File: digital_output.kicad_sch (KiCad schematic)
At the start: 13 parts, among them J4 Molex MicroFit 2x2, Q13 PMOS, Q9 PMOS

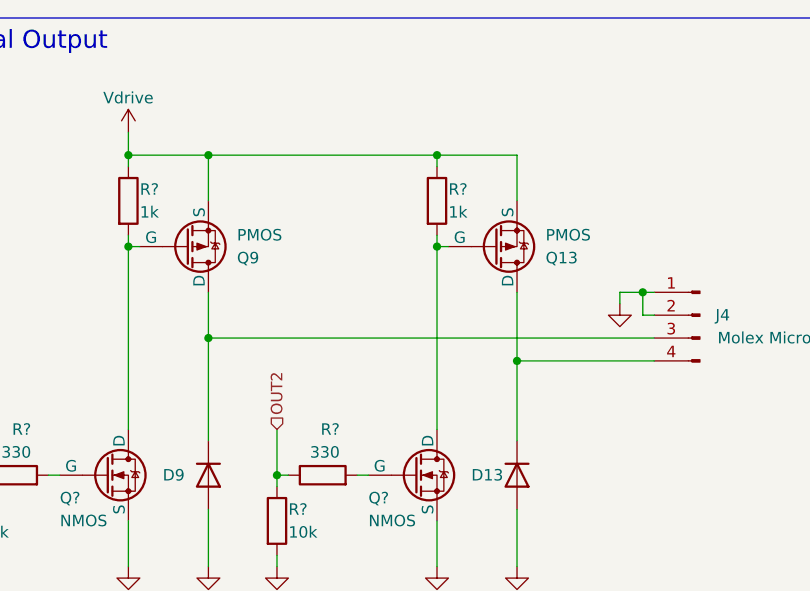
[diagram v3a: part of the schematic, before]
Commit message: updates to the schematics, rough component placement in the PCB layout
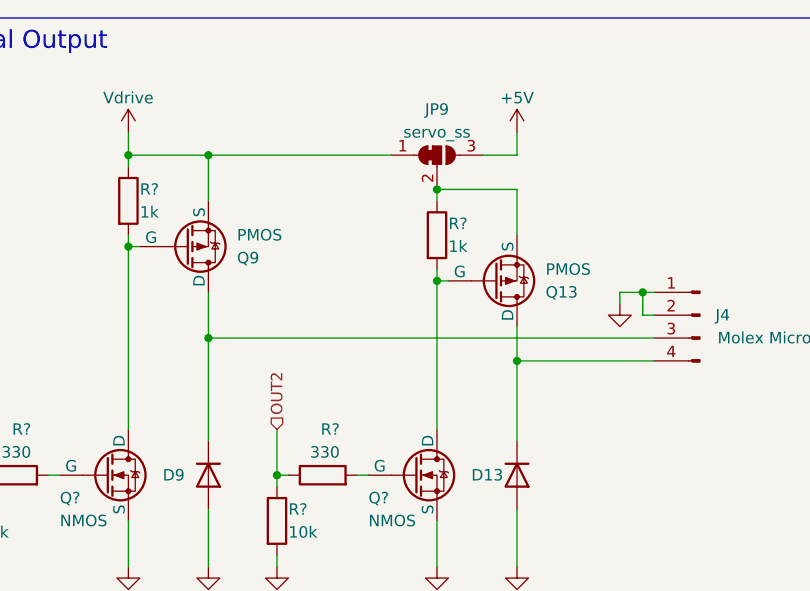
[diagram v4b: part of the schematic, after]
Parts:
- added JP9: servo_ss, Jumper:SolderJumper-3_P1.3mm_Open_RoundedPad1.0x1.5mm, symbol Jumper:SolderJumper_3_Bridged12
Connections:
- net Vdrive: now also JP9.1 (A); no longer Q13.3 (S), R?.1
- new net: JP9.2 (C), Q13.3 (S), R?.1
- new net +5V: JP9.3 (B)
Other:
- moved on the sheet: Q13, R?
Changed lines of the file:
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@@
   (junction (at 93.98 44.45) (diameter 0) (color 0 0 0 0)
   )
-  (junction (at 71.12 39.37) (diameter 0) (color 0 0 0 0)
-  )
   (junction (at 36.83 29.21) (diameter 0) (color 0 0 0 0)
   )
@@
   (junction (at 53.34 64.77) (diameter 0) (color 0 0 0 0)
   )
-  (junction (at 71.12 29.21) (diameter 0) (color 0 0 0 0)
+  (junction (at 71.12 33.02) (diameter 0) (color 0 0 0 0)
   )
   (junction (at 45.72 49.53) (diameter 0) (color 0 0 0 0)
@@
   (junction (at 36.83 39.37) (diameter 0) (color 0 0 0 0)
   )
+  (junction (at 71.12 43.18) (diameter 0) (color 0 0 0 0)
+  )
   (wire (pts (xy 36.83 39.37) (xy 36.83 38.1))
     (stroke (width 0) (type default))
@@
     (stroke (width 0) (type default))
   )
+  (wire (pts (xy 71.12 33.02) (xy 71.12 34.29))
+    (stroke (width 0) (type default))
+  )
   (wire (pts (xy 45.72 34.29) (xy 45.72 29.21))
     (stroke (width 0) (type default))
   )
+  (wire (pts (xy 76.2 29.21) (xy 80.01 29.21))
+    (stroke (width 0) (type default))
+  )
   (wire (pts (xy 80.01 68.58) (xy 80.01 74.93))
     (stroke (width 0) (type default))
@@
     (stroke (width 0) (type default))
   )
+  (wire (pts (xy 80.01 29.21) (xy 80.01 26.67))
+    (stroke (width 0) (type default))
+  )
   (wire (pts (xy 19.05 59.69) (xy 19.05 64.77))
     (stroke (width 0) (type default))
@@
     (stroke (width 0) (type default))
   )
-  (wire (pts (xy 71.12 38.1) (xy 71.12 39.37))
-    (stroke (width 0) (type default))
-  )
   (wire (pts (xy 45.72 44.45) (xy 45.72 49.53))
     (stroke (width 0) (type default))
@@
     (stroke (width 0) (type default))
   )
-  (wire (pts (xy 80.01 29.21) (xy 71.12 29.21))
+  (wire (pts (xy 71.12 33.02) (xy 80.01 33.02))
     (stroke (width 0) (type default))
   )
@@
     (stroke (width 0) (type default))
   )
-  (wire (pts (xy 80.01 34.29) (xy 80.01 29.21))
+  (wire (pts (xy 80.01 38.1) (xy 80.01 33.02))
     (stroke (width 0) (type default))
   )
@@
     (stroke (width 0) (type default))
   )
-  (wire (pts (xy 80.01 44.45) (xy 80.01 52.07))
+  (wire (pts (xy 80.01 48.26) (xy 80.01 52.07))
+    (stroke (width 0) (type default))
+  )
+  (wire (pts (xy 71.12 43.18) (xy 71.12 59.69))
     (stroke (width 0) (type default))
   )
@@
     (stroke (width 0) (type default))
   )
-  (wire (pts (xy 71.12 29.21) (xy 45.72 29.21))
-    (stroke (width 0) (type default))
-  )
   (wire (pts (xy 36.83 26.67) (xy 36.83 29.21))
     (stroke (width 0) (type default))
@@
     (stroke (width 0) (type default))
   )
+  (wire (pts (xy 45.72 29.21) (xy 66.04 29.21))
+    (stroke (width 0) (type default))
+  )
   (wire (pts (xy 53.34 59.69) (xy 53.34 64.77))
     (stroke (width 0) (type default))
@@
     (stroke (width 0) (type default))
   )
-  (wire (pts (xy 71.12 29.21) (xy 71.12 30.48))
-    (stroke (width 0) (type default))
-  )
   (wire (pts (xy 19.05 64.77) (xy 20.32 64.77))
     (stroke (width 0) (type default))
   )
-  (wire (pts (xy 71.12 39.37) (xy 71.12 59.69))
+  (wire (pts (xy 71.12 41.91) (xy 71.12 43.18))
     (stroke (width 0) (type default))
   )
@@
     (stroke (width 0) (type default))
   )
-  (wire (pts (xy 71.12 39.37) (xy 72.39 39.37))
+  (wire (pts (xy 71.12 43.18) (xy 72.39 43.18))
     (stroke (width 0) (type default))
   )
@@
     )
   )
-  (symbol (lib_id "Device:R") (at 71.12 34.29 0) (unit 1)
-    (in_bom yes) (on_board yes) (dnp no)
-    (property "Reference" "R?" (at 72.39 33.02 0)
-      (effects (font (size 1.27 1.27)) (justify left))
-    )
-    (property "Value" "1k" (at 72.39 35.56 0)
-      (effects (font (size 1.27 1.27)) (justify left))
-    )
-    (property "Footprint" "Resistor_SMD:R_0603_1608Metric_Pad0.98x0.95mm_HandSolder" (at 69.342 34.29 90)
-      (effects (font (size 1.27 1.27)) hide)
-    )
-    (property "Datasheet" "~" (at 71.12 34.29 0)
+  (symbol (lib_id "Device:R") (at 71.12 38.1 0) (unit 1)
+    (in_bom yes) (on_board yes) (dnp no)
+    (property "Reference" "R?" (at 72.39 36.83 0)
+      (effects (font (size 1.27 1.27)) (justify left))
+    )
+    (property "Value" "1k" (at 72.39 39.37 0)
+      (effects (font (size 1.27 1.27)) (justify left))
+    )
+    (property "Footprint" "Resistor_SMD:R_0603_1608Metric_Pad0.98x0.95mm_HandSolder" (at 69.342 38.1 90)
+      (effects (font (size 1.27 1.27)) hide)
+    )
+    (property "Datasheet" "~" (at 71.12 38.1 0)
       (effects (font (size 1.27 1.27)) hide)
     )
@@
     )
   )
+  (symbol (lib_id "Jumper:SolderJumper_3_Bridged12") (at 71.12 29.21 0) (unit 1)
+    (in_bom yes) (on_board yes) (dnp no)
+    (property "Reference" "JP9" (at 71.12 24.13 0)
+      (effects (font (size 1.27 1.27)))
+    )
+    (property "Value" "servo_ss" (at 71.12 26.67 0)
+      (effects (font (size 1.27 1.27)))
+    )
+    (property "Footprint" "Jumper:SolderJumper-3_P1.3mm_Open_RoundedPad1.0x1.5mm" (at 71.12 29.21 0)
+      (effects (font (size 1.27 1.27)) hide)
+    )
+    (property "Datasheet" "~" (at 71.12 29.21 0)
+      (effects (font (size 1.27 1.27)) hide)
+    )
+    (pin "2")
+    (pin "3")
+    (pin "1")
+    (instances
+      (project "frodo_io_module"
+        (path "/c1ccca3c-4648-4b8e-86a1-690c24c5f13e/1daa12b0-ccec-42a7-b3b8-2333aafbd367"
+          (reference "JP9") (unit 1)
+        )
+        (path "/c1ccca3c-4648-4b8e-86a1-690c24c5f13e/3f7b9377-485e-4135-be49-570466b5bb08"
+          (reference "JP10") (unit 1)
+        )
+        (path "/c1ccca3c-4648-4b8e-86a1-690c24c5f13e/d1a2137e-7321-491e-b4c1-a40d594ed11a"
+          (reference "JP11") (unit 1)
+        )
+        (path "/c1ccca3c-4648-4b8e-86a1-690c24c5f13e/622092df-af96-403b-81ea-4936d38e5a4c"
+          (reference "JP12") (unit 1)
+        )
+      )
+    )
+  )
   (symbol (lib_id "power:GND") (at 53.34 74.93 0) (unit 1)
     (in_bom yes) (on_board yes) (dnp no) (fields_autoplaced)
@@
     )
   )
+  (symbol (lib_id "power:+5V") (at 80.01 26.67 0) (unit 1)
+    (in_bom yes) (on_board yes) (dnp no)
+    (property "Reference" "#PWR084" (at 80.01 30.48 0)
+      (effects (font (size 1.27 1.27)) hide)
+    )
+    (property "Value" "+5V" (at 80.01 22.86 0)
+      (effects (font (size 1.27 1.27)))
+    )
+    (property "Footprint" "" (at 80.01 26.67 0)
+      (effects (font (size 1.27 1.27)) hide)
+    )
+    (property "Datasheet" "" (at 80.01 26.67 0)
+      (effects (font (size 1.27 1.27)) hide)
+    )
+    (pin "1")
+    (instances
+      (project "frodo_io_module"
+        (path "/c1ccca3c-4648-4b8e-86a1-690c24c5f13e"
+          (reference "#PWR084") (unit 1)
+        )
+        (path "/c1ccca3c-4648-4b8e-86a1-690c24c5f13e/1daa12b0-ccec-42a7-b3b8-2333aafbd367"
+          (reference "#PWR0117") (unit 1)
+        )
+        (path "/c1ccca3c-4648-4b8e-86a1-690c24c5f13e/3f7b9377-485e-4135-be49-570466b5bb08"
+          (reference "#PWR0118") (unit 1)
+        )
+        (path "/c1ccca3c-4648-4b8e-86a1-690c24c5f13e/d1a2137e-7321-491e-b4c1-a40d594ed11a"
+          (reference "#PWR0119") (unit 1)
+        )
+        (path "/c1ccca3c-4648-4b8e-86a1-690c24c5f13e/622092df-af96-403b-81ea-4936d38e5a4c"
+          (reference "#PWR0120") (unit 1)
+        )
+      )
+    )
+  )
   (symbol (lib_id "Simulation_SPICE:NMOS") (at 34.29 64.77 0) (unit 1)
     (in_bom yes) (on_board yes) (dnp no)
@@
     )
   )
-  (symbol (lib_id "Simulation_SPICE:PMOS") (at 77.47 39.37 0) (mirror x) (unit 1)
-    (in_bom yes) (on_board yes) (dnp no)
-    (property "Reference" "Q13" (at 83.185 40.64 0)
-      (effects (font (size 1.27 1.27)) (justify left))
-    )
-    (property "Value" "PMOS" (at 83.185 38.1 0)
-      (effects (font (size 1.27 1.27)) (justify left))
-    )
-    (property "Footprint" "Package_TO_SOT_SMD:SOT-23" (at 82.55 41.91 0)
-      (effects (font (size 1.27 1.27)) hide)
-    )
-    (property "Datasheet" "https://ngspice.sourceforge.io/docs/ngspice-manual.pdf" (at 77.47 26.67 0)
-      (effects (font (size 1.27 1.27)) hide)
-    )
-    (property "Sim.Device" "PMOS" (at 77.47 22.225 0)
-      (effects (font (size 1.27 1.27)) hide)
-    )
-    (property "Sim.Type" "VDMOS" (at 77.47 20.32 0)
-      (effects (font (size 1.27 1.27)) hide)
-    )
-    (property "Sim.Pins" "1=D 2=G 3=S" (at 77.47 24.13 0)
-      (effects (font (size 1.27 1.27)) hide)
-    )
+  (symbol (lib_id "Simulation_SPICE:PMOS") (at 77.47 43.18 0) (mirror x) (unit 1)
+    (in_bom yes) (on_board yes) (dnp no)
+    (property "Reference" "Q13" (at 83.185 44.45 0)
+      (effects (font (size 1.27 1.27)) (justify left))
+    )
+    (property "Value" "PMOS" (at 83.185 41.91 0)
+      (effects (font (size 1.27 1.27)) (justify left))
+    )
+    (property "Footprint" "Package_TO_SOT_SMD:SOT-23" (at 82.55 45.72 0)
+      (effects (font (size 1.27 1.27)) hide)
+    )
+    (property "Datasheet" "https://ngspice.sourceforge.io/docs/ngspice-manual.pdf" (at 77.47 30.48 0)
+      (effects (font (size 1.27 1.27)) hide)
+    )
+    (property "Sim.Device" "PMOS" (at 77.47 26.035 0)
+      (effects (font (size 1.27 1.27)) hide)
+    )
+    (property "Sim.Type" "VDMOS" (at 77.47 24.13 0)
+      (effects (font (size 1.27 1.27)) hide)
+    )
+    (property "Sim.Pins" "1=D 2=G 3=S" (at 77.47 27.94 0)
+      (effects (font (size 1.27 1.27)) hide)
+    )
